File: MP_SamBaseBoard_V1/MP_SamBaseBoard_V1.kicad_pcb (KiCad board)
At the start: 4 copper layers, 80 x 60 mm, 132 parts, among them J1 MA_CONN, J10 P1_CONN, J11 I2C_CONN, J12 I2C_CONN, J13 SAM_SWD, J14 WS2812_EXT, J15 PWR_JACK, J16 USB_B_Micro, J17 BATT_CONN, J2 MB_CONN, J3 Adafruit_Feather_CONN, J4 LOAD_CONN, J5 SPEAKER, J7 SERVO_CONN, J8 P3_CONN, J9 P2_CONN, Q1 DMP3098L, Q2 ALS-PT19-315C/L177/TR8, Q3 BSS138-7-F, SW1 RESET, SW2 3v3_PWR_SW, SW3 SW1, SW4 SW2, U1 ESP32-WROOM-32, U10 KXTJ3-1057, U11 IRFHM3911PbF, U12 IRFHM9331PbF, U13 SST25VF016B-50-4C-S2AF, U14 IRFHM9331PbF, U2 ATSAMD51J19A-A, U3 74LVC1G125, U4 TPS62135, U5 PAM8301, U6 BQ24075, U7 DRV8833RTY, U8 Sensirion_SHT3x, U9 LD39200PU33R, Y1 Crystal

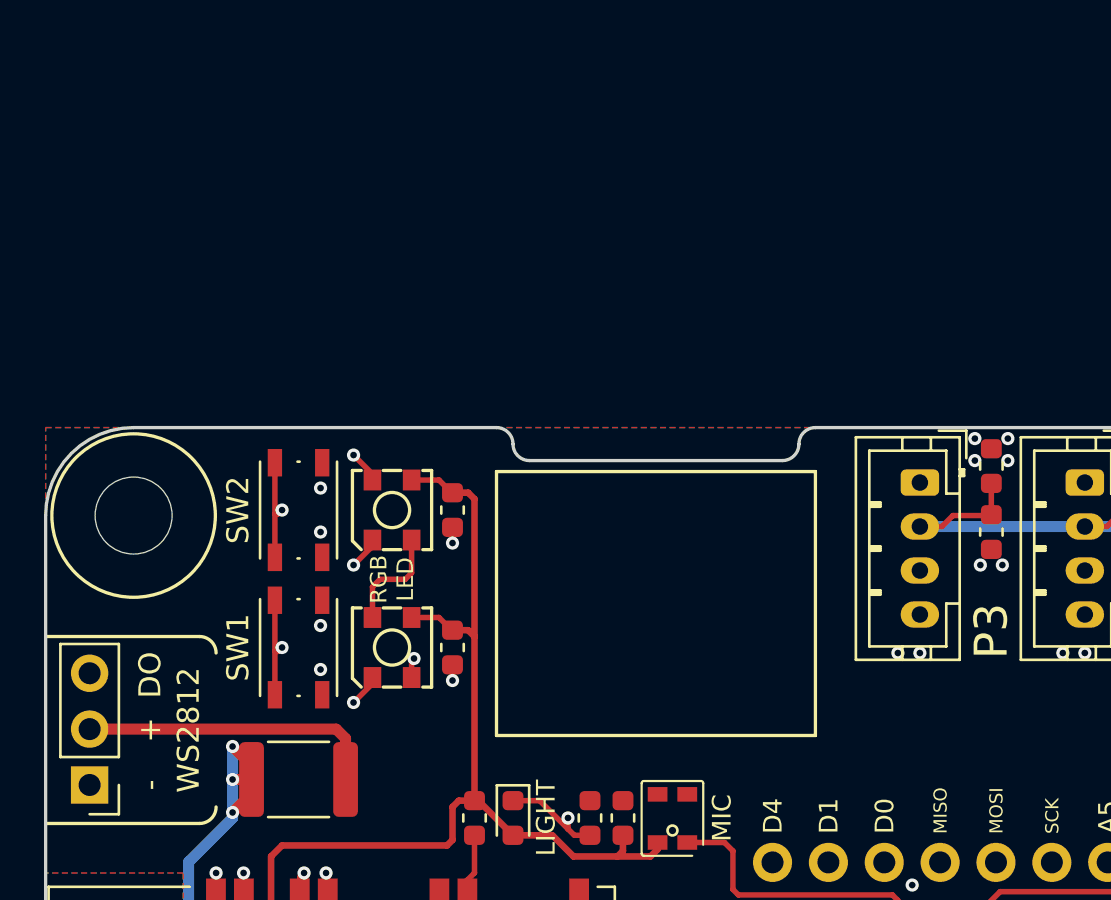
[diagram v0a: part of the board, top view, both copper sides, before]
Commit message: Update OLED display, not complete
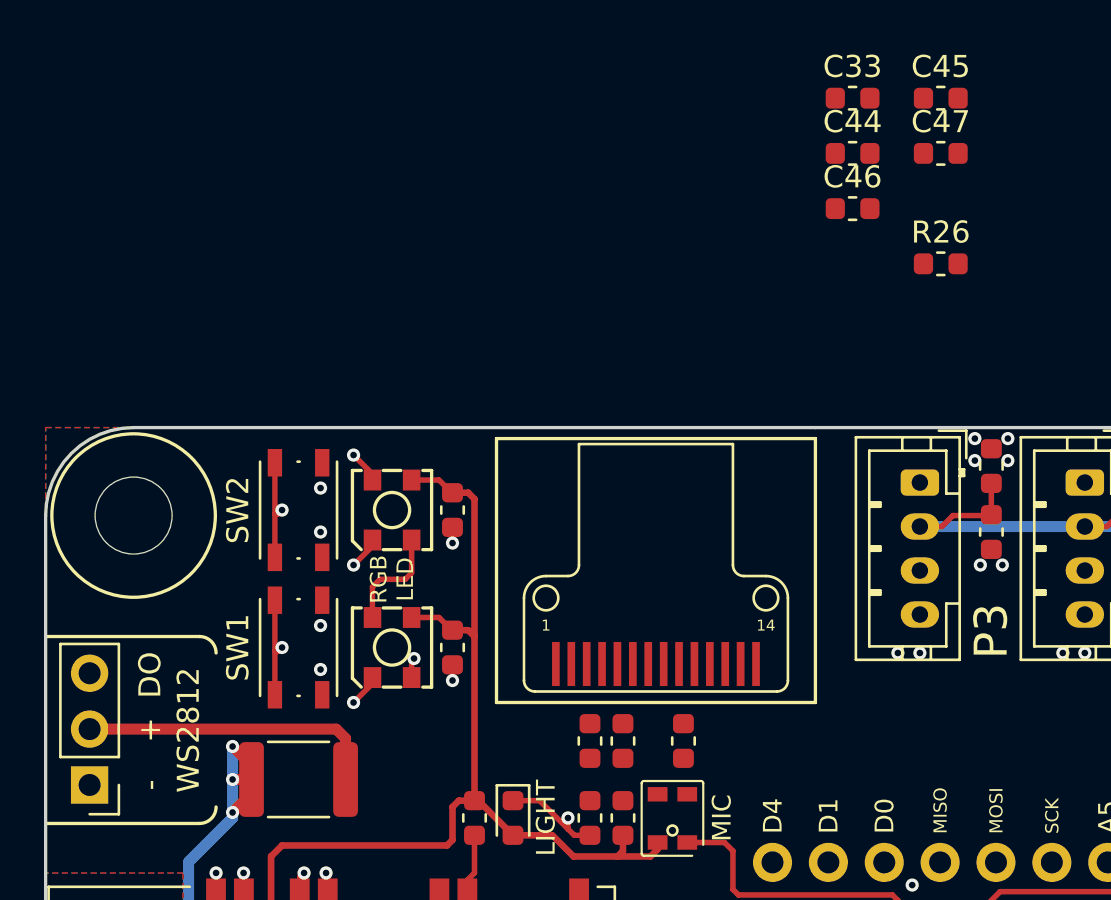
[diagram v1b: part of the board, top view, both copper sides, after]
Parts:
- added C33: 4.7uF, Capacitor_SMD:C_0603_1608Metric, F.Cu at (161.7, 57.5)
- added C44: 0.1uF, Capacitor_SMD:C_0603_1608Metric, F.Cu at (161.7, 60.0)
- added C45: 4.7uF, Capacitor_SMD:C_0603_1608Metric, F.Cu at (165.7, 57.5)
- added C46: 0.1uF, Capacitor_SMD:C_0603_1608Metric, F.Cu at (161.7, 62.5)
- added C47: 2.2uF, Capacitor_SMD:C_0603_1608Metric, F.Cu at (165.7, 60.0)
- added C48: 1uF, Capacitor_SMD:C_0603_1608Metric, F.Cu at (149.8, 86.8)
- added C49: 1uF, Capacitor_SMD:C_0603_1608Metric, F.Cu at (151.2, 86.8)
- added OLED1: WiseChip-VG-6432TSWAG01, GiraffeTech-Connector:WiseChip-VG-6432TSWAG01, F.Cu at (152.8, 78.2)
- added R25: 10K, Resistor_SMD:R_0603_1608Metric, F.Cu at (154.0, 86.8)
- added R26: 560K, Resistor_SMD:R_0603_1608Metric, F.Cu at (165.7, 65.1)
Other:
- outline, holes or cut-outs redrawn

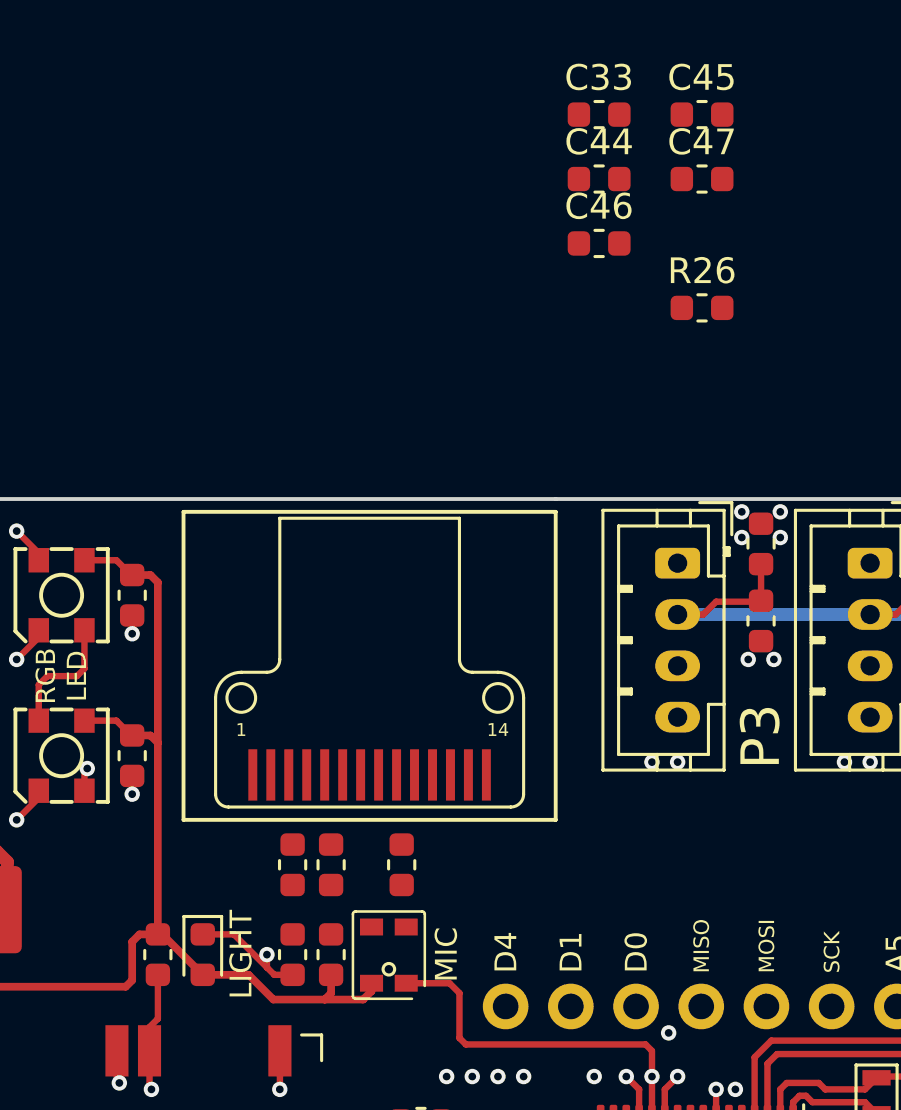
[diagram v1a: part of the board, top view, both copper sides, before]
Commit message: Finalize OLED footprint placement
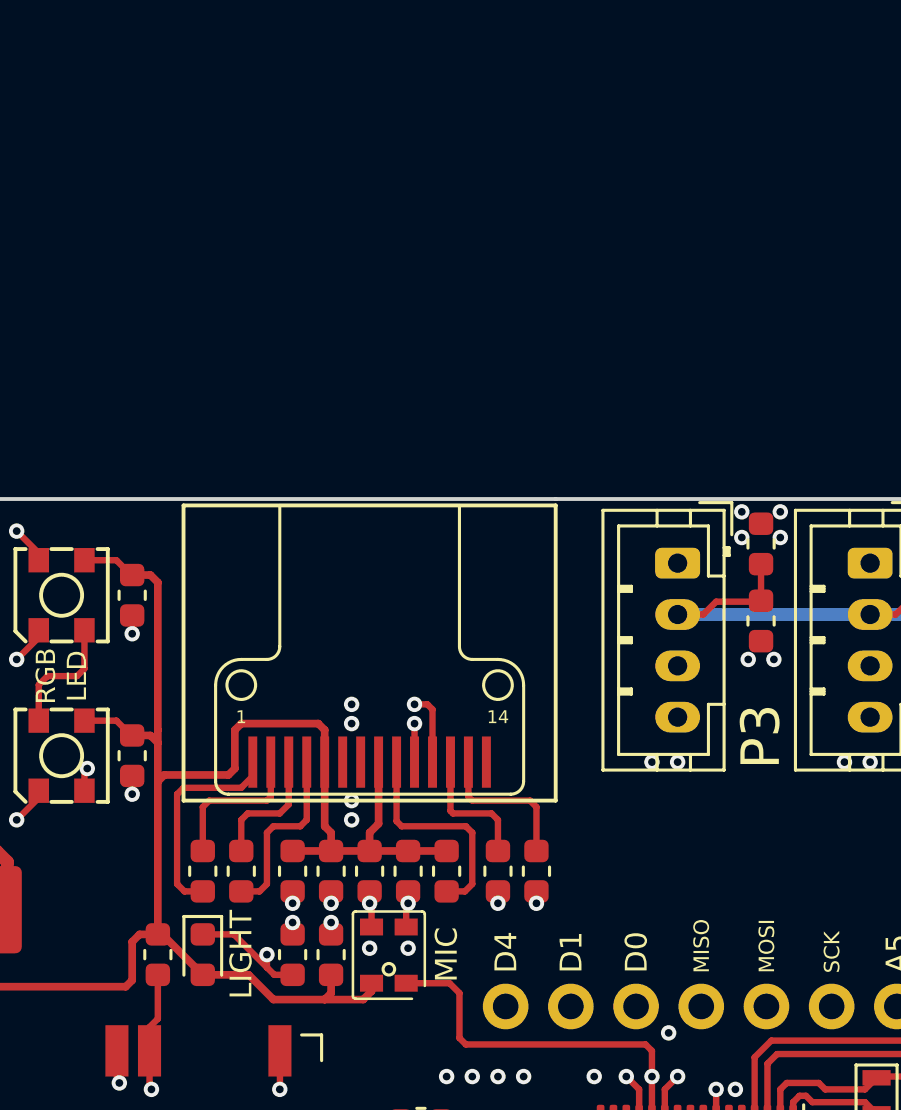
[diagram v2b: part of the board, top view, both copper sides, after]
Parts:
- moved C45 33.5 mm to (149.8, 87.0), turned to 90 degrees
- moved C33 30.4 mm to (154.2, 87.0), turned to 90 degrees
- moved C44 28.4 mm to (152.8, 87.0), turned to 90 degrees
- moved C47 27.7 mm to (159.2, 87.0), turned to 90 degrees
- moved C46 26.6 mm to (151.2, 87.0), turned to 90 degrees
- moved R26 23.3 mm to (157.8, 87.0), turned to 270 degrees
- moved C48 3.51 mm to (146.2, 87.0)
- moved C49 3.51 mm to (147.8, 87.0), turned to 270 degrees
- moved R25 1.77 mm to (155.8, 87.0), turned to 90 degrees
- moved OLED1 0.50 mm to (152.8, 77.8)
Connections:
- C33 pad 2: VCC_OEL -> +3V3
- C44 pad 2: VCC_OEL -> +3V3
- C45 pad 2: VDD_LOGIC -> +3V3
- C46 pad 2: VDD_LOGIC -> +3V3
- OLED1 pad 14: VCC_OEL -> (no net)
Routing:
- net I2C_SDA: track 106.7 -> 147.7 mm, vias 2 -> 3
- net I2C_SCL: track 99.8 -> 137.9 mm, vias 2 -> 3
- net +3V3: track 446.9 -> 469.7 mm
- net Net-(OLED1-Pad9): track 0.00 -> 8.56 mm
- net Net-(C48-Pad1): track 0.00 -> 8.41 mm
- net Net-(C49-Pad2): track 0.00 -> 7.13 mm
- net Net-(C48-Pad2): track 0.00 -> 5.88 mm
- net VCOMH: track 0.00 -> 5.88 mm
- net GND: track 65.1 -> 70.2 mm, vias 188 -> 202
- net IREF: track 0.00 -> 5.11 mm
- net Net-(C49-Pad1): track 0.00 -> 4.96 mm

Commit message: update
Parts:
- added G***: LOGO, GiraffeTech-Utility:InGarage_Logo, B.Cu at (128.2, 102.5)
- added REF**: Symbol_Barrel_Polarity, Symbol:Symbol_Barrel_Polarity, F.Cu at (186.5, 128.3)
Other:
- board text added: "V1.0"
- board text removed: "3.7V Li-PO Li-ION"
- board text removed: "9-15 VDC"
- board text removed: "LOAD"
- board text removed: "SW"
- board text removed: "V0.1"
